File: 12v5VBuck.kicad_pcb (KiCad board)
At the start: 4 copper layers, 20.5 x 26 mm, 17 parts, among them IC1 TPS54302DDCT, J1 Conn_01x02, J2 Conn_01x02

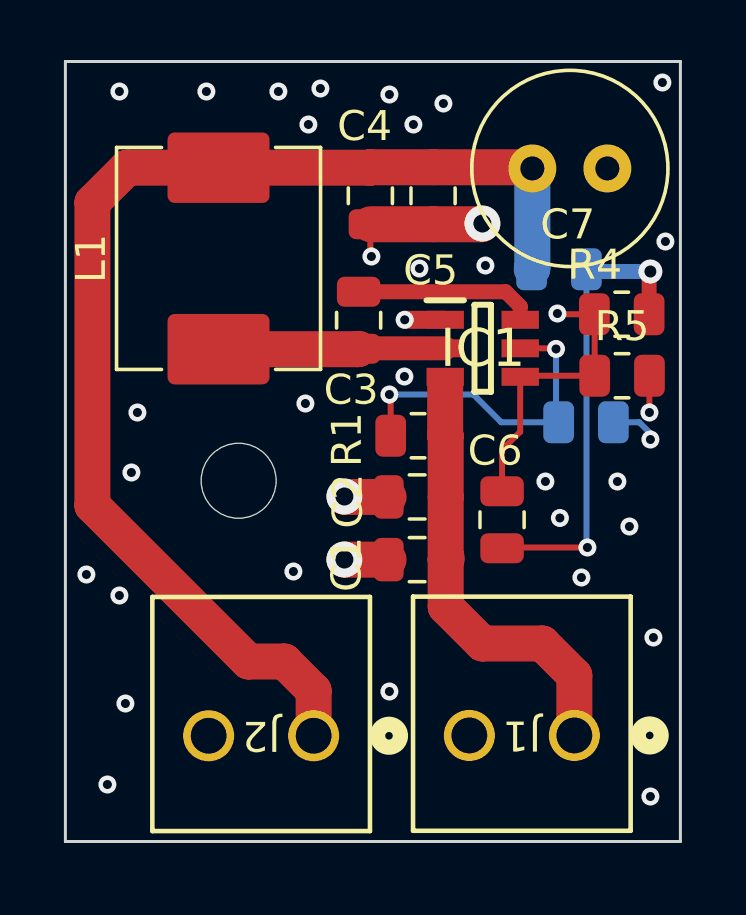
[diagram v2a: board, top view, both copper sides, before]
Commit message: Minor changes to traces
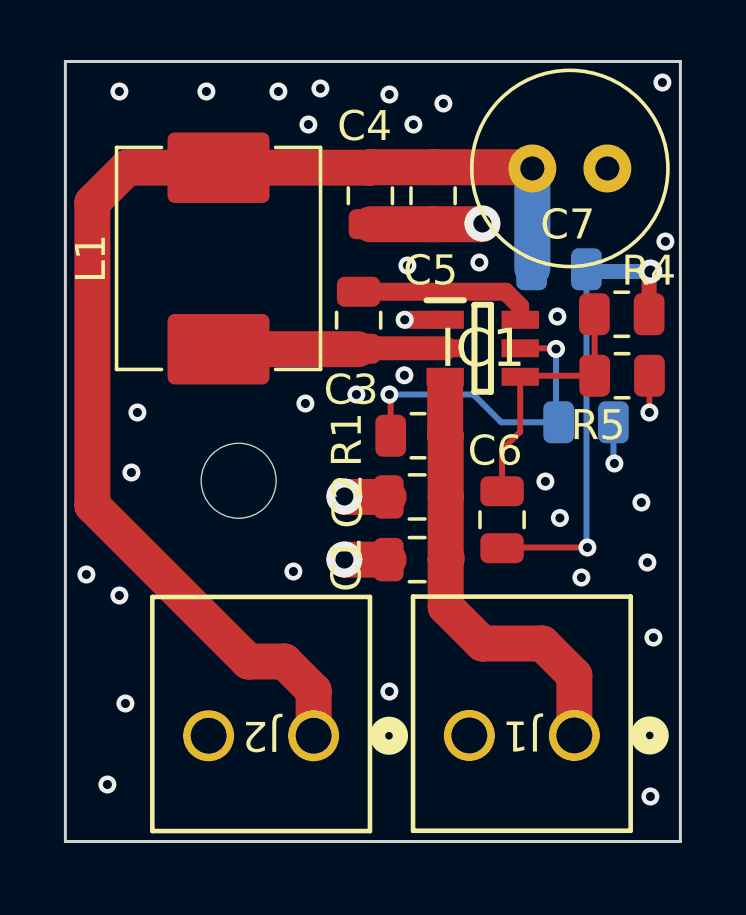
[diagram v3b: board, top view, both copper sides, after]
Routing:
- net Net-(IC1-FB): track 9.86 -> 8.60 mm, vias 1 -> 0
- net GND: track 11.9 -> 10.7 mm, vias 36 -> 37
- net Net-(IC1-BOOT): track 5.54 -> 6.04 mm
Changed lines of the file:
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@@
     (property "ki_keywords" "r resistor")
     (attr smd)
-    (fp_text reference "R5" (at 0 -1.65) (layer "F.SilkS")
+    (fp_text reference "R5" (at -0.8 1.65) (layer "F.SilkS")
         (effects (font (size 1 1) (thickness 0.15)))
     )
@@
       (rotate (xyz 0 0 0))
     )
+    (model "C:/Users/Sylvester Pudelko/Documents/KiCad/7.0/3dmodels/DDC0006A.stp"
+      (offset (xyz 0 0 0))
+      (scale (xyz 1 1 1))
+      (rotate (xyz 0 0 0))
+    )
   )
   (footprint "Capacitor_SMD:C_0805_2012Metric" (layer "F.Cu")
@@
     (property "ki_keywords" "r resistor")
     (attr smd)
-    (fp_text reference "R4" (at 0.9 1.65) (layer "F.SilkS")
+    (fp_text reference "R4" (at -0.9 1.45) (layer "F.SilkS")
         (effects (font (size 1 1) (thickness 0.15)))
     )
@@
   (segment (start 63.815 29.115) (end 63.8 29.1) (width 1.2) (layer "F.Cu") (net 2))
   (segment (start 66.755 20.025) (end 68.375 20.025) (width 1.2) (layer "F.Cu") (net 2))
-  (segment (start 64.665 20.025) (end 64.665 21.065) (width 0.2) (layer "F.Cu") (net 2))
   (segment (start 68.375 20.025) (end 68.4 20) (width 1.2) (layer "F.Cu") (net 2))
   (segment (start 73.9675 26.3) (end 73.9675 25.075) (width 0.2) (layer "F.Cu") (net 2))
@@
   (segment (start 63.805 31.205) (end 63.8 31.2) (width 1.2) (layer "F.Cu") (net 2))
   (segment (start 65.275 31.205) (end 63.805 31.205) (width 1.2) (layer "F.Cu") (net 2))
-  (via (at 65.8 25.1) (size 0.6) (drill 0.3) (layers "F.Cu" "B.Cu") (net 2))
-  (via (at 66.3 21.5) (size 0.6) (drill 0.3) (layers "F.Cu" "B.Cu") (net 2))
+  (via (at 65.8 25.0595) (size 0.6) (drill 0.3) (layers "F.Cu" "B.Cu") (net 2))
   (via (at 56.9 26.3) (size 0.6) (drill 0.3) (layers "F.Cu" "B.Cu") (net 2))
   (via (at 56.3 15.6) (size 0.6) (drill 0.3) (layers "F.Cu" "B.Cu") (net 2))
+  (via (at 70.9 23.1) (size 0.6) (drill 0.3) (layers "F.Cu" "B.Cu") (net 2))
   (via (at 65.81 23.21) (size 0.6) (drill 0.3) (layers "F.Cu" "B.Cu") (net 2))
   (via (at 56.7 28.3) (size 0.6) (drill 0.3) (layers "F.Cu" "B.Cu") (net 2))
@@
   (via (at 62.1 31.6) (size 0.6) (drill 0.3) (layers "F.Cu" "B.Cu") (net 2))
   (via (at 74 39.1) (size 0.6) (drill 0.3) (layers "F.Cu" "B.Cu") (net 2))
-  (via (at 68.5 21.4) (size 0.6) (drill 0.3) (layers "F.Cu" "B.Cu") (net 2))
   (via (at 67.1 16) (size 0.6) (drill 0.3) (layers "F.Cu" "B.Cu") (net 2))
-  (via (at 72.9 28.6) (size 0.6) (drill 0.3) (layers "F.Cu" "B.Cu") (net 2))
+  (via (at 73.7 29.3) (size 0.6) (drill 0.3) (layers "F.Cu" "B.Cu") (net 2))
   (via (at 74.4 15.3) (size 0.6) (drill 0.3) (layers "F.Cu" "B.Cu") (net 2))
+  (via (at 65.9 21.4) (size 0.6) (drill 0.3) (layers "F.Cu" "B.Cu") (net 2))
   (via (at 70.5 28.6) (size 0.6) (drill 0.3) (layers "F.Cu" "B.Cu") (net 2))
   (via (at 66.1 16.7) (size 0.6) (drill 0.3) (layers "F.Cu" "B.Cu") (net 2))
-  (via (at 73.3 30.1) (size 0.6) (drill 0.3) (layers "F.Cu" "B.Cu") (net 2))
+  (via (at 73.9 31.3) (size 0.6) (drill 0.3) (layers "F.Cu" "B.Cu") (net 2))
   (via (at 63.8 29.1) (size 1.2) (drill 0.6) (layers "F.Cu" "B.Cu") (net 2))
+  (via (at 64.2 25.7) (size 0.6) (drill 0.3) (layers "F.Cu" "B.Cu") (net 2))
   (via (at 55.2 31.7) (size 0.6) (drill 0.3) (layers "F.Cu" "B.Cu") (net 2))
   (via (at 63.8 31.2) (size 1.2) (drill 0.6) (layers "F.Cu" "B.Cu") (net 2))
   (via (at 61.6 15.6) (size 0.6) (drill 0.3) (layers "F.Cu" "B.Cu") (net 2))
-  (via (at 74 27.2) (size 0.6) (drill 0.3) (layers "F.Cu" "B.Cu") (net 2))
+  (via (at 72.8 28) (size 0.6) (drill 0.3) (layers "F.Cu" "B.Cu") (net 2))
   (via (at 62.5 26) (size 0.6) (drill 0.3) (layers "F.Cu" "B.Cu") (net 2))
-  (via (at 64.7 21.1) (size 0.6) (drill 0.3) (layers "F.Cu" "B.Cu") (net 2))
   (via (at 74.1 33.8) (size 0.6) (drill 0.3) (layers "F.Cu" "B.Cu") (net 2))
   (via (at 56.5 36) (size 0.6) (drill 0.3) (layers "F.Cu" "B.Cu") (net 2))
@@
   (via (at 65.3 35.6) (size 0.6) (drill 0.3) (layers "F.Cu" "B.Cu") (net 2))
   (via (at 59.2 15.6) (size 0.6) (drill 0.3) (layers "F.Cu" "B.Cu") (net 2))
+  (via (at 68.3 21.3) (size 0.6) (drill 0.3) (layers "F.Cu" "B.Cu") (net 2))
   (via (at 73.9675 26.3) (size 0.6) (drill 0.3) (layers "F.Cu" "B.Cu") (net 2))
   (via (at 74.5 20.6) (size 0.6) (drill 0.3) (layers "F.Cu" "B.Cu") (net 2))
   (via (at 65.3 15.7) (size 0.6) (drill 0.3) (layers "F.Cu" "B.Cu") (net 2))
-  (segment (start 73.625 26.625) (end 74 27) (width 0.2) (layer "B.Cu") (net 2))
-  (segment (start 74 27) (end 74 27.2) (width 0.2) (layer "B.Cu") (net 2))
-  (segment (start 72.7675 26.625) (end 73.625 26.625) (width 0.2) (layer "B.Cu") (net 2))
-  (segment (start 69.66 22.76) (end 69.175 22.275) (width 0.5) (layer "F.Cu") (net 3))
-  (segment (start 69.175 22.275) (end 64.775 22.275) (width 0.5) (layer "F.Cu") (net 3))
-  (segment (start 69.66 23.21) (end 69.66 22.76) (width 0.5) (layer "F.Cu") (net 3))
-  (segment (start 67.16 24.16) (end 64.79 24.16) (width 0.8) (layer "F.Cu") (net 4))
-  (segment (start 64.79 24.16) (end 64.775 24.175) (width 0.8) (layer "F.Cu") (net 4))
-  (segment (start 64.26 24.19) (end 64.275 24.175) (width 1.2) (layer "F.Cu") (net 4))
+  (segment (start 72.8 28) (end 72.7675 27.9675) (width 0.2) (layer "B.Cu") (net 2))
+  (segment (start 72.7675 27.9675) (end 72.7675 26.625) (width 0.2) (layer "B.Cu") (net 2))
+  (segment (start 64.275 22.275) (end 69.175 22.275) (width 0.6) (layer "F.Cu") (net 3))
+  (segment (start 69.175 22.275) (end 69.66 22.76) (width 0.6) (layer "F.Cu") (net 3))
+  (segment (start 69.66 22.76) (end 69.66 23.21) (width 0.6) (layer "F.Cu") (net 3))
   (segment (start 59.605 24.19) (end 64.26 24.19) (width 1.2) (layer "F.Cu") (net 4))
-  (segment (start 59.92 24.175) (end 59.905 24.19) (width 1.2) (layer "F.Cu") (net 4))
+  (segment (start 67.16 24.16) (end 64.29 24.16) (width 0.8) (layer "F.Cu") (net 4))
   (segment (start 73.9575 23.025) (end 73.9575 21.6425) (width 0.5) (layer "F.Cu") (net 5))
   (segment (start 69.08 30.8) (end 69.055 30.825) (width 0.2) (layer "F.Cu") (net 5))
@@
   (segment (start 72.1425 21.6) (end 71.8675 21.325) (width 0.5) (layer "B.Cu") (net 5))
   (segment (start 69.695 25.075) (end 69.66 25.11) (width 0.2) (layer "F.Cu") (net 6))
-  (segment (start 70.925 23.025) (end 70.9 23) (width 0.2) (layer "F.Cu") (net 6))
   (segment (start 69.055 28.925) (end 69.055 27.545) (width 0.2) (layer "F.Cu") (net 6))
   (segment (start 69.66 26.94) (end 69.66 25.11) (width 0.2) (layer "F.Cu") (net 6))
   (segment (start 69.055 27.545) (end 69.66 26.94) (width 0.2) (layer "F.Cu") (net 6))
-  (segment (start 72.1325 23.025) (end 70.925 23.025) (width 0.2) (layer "F.Cu") (net 6))
   (segment (start 72.1425 25.075) (end 72.1425 23.035) (width 0.2) (layer "F.Cu") (net 6))
   (segment (start 72.1425 25.075) (end 69.695 25.075) (width 0.2) (layer "F.Cu") (net 6))
-  (segment (start 72.1425 23.035) (end 72.1325 23.025) (width 0.2) (layer "F.Cu") (net 6))
-  (via (at 70.9 23) (size 0.6) (drill 0.3) (layers "F.Cu" "B.Cu") (net 6))
   (segment (start 70.8546 24.181601) (end 70.832999 24.16) (width 0.2) (layer "F.Cu") (net 7))
   (segment (start 65.3425 27.075) (end 65.3425 25.7425) (width 0.2) (layer "F.Cu") (net 7))
@@
   (via (at 70.8546 24.181601) (size 0.6) (drill 0.3) (layers "F.Cu" "B.Cu") (net 7))
   (via (at 65.3 25.7) (size 0.6) (drill 0.3) (layers "F.Cu" "B.Cu") (net 7))
-  (segment (start 70.8546 24.181601) (end 70.8546 26.4371) (width 0.2) (layer "B.Cu") (net 7))
   (segment (start 65.3 25.7) (end 68.1 25.7) (width 0.2) (layer "B.Cu") (net 7))
   (segment (start 68.1 25.7) (end 69.025 26.625) (width 0.2) (layer "B.Cu") (net 7))
-  (segment (start 70.8546 26.4371) (end 71.0425 26.625) (width 0.2) (layer "B.Cu") (net 7))
   (segment (start 69.025 26.625) (end 70.9425 26.625) (width 0.2) (layer "B.Cu") (net 7))
+  (segment (start 70.8546 24.181601) (end 70.8546 26.5371) (width 0.2) (layer "B.Cu") (net 7))
   (segment (start 61.8 34.6) (end 60.6 34.6) (width 1.2) (layer "F.Cu") (net 8))
   (segment (start 64.65 18.14) (end 64.665 18.125) (width 1.2) (layer "F.Cu") (net 8))
@@
   (segment (start 70.025 18.125) (end 70.065 18.165) (width 1.2) (layer "F.Cu") (net 8))
   (segment (start 64.665 18.125) (end 66.755 18.125) (width 1.2) (layer "F.Cu") (net 8))
-  (segment (start 70.065 21.5025) (end 70.0425 21.525) (width 1.2) (layer "B.Cu") (net 8))
   (segment (start 70.065 18.165) (end 70.065 21.5025) (width 1.2) (layer "B.Cu") (net 8))
   (zone (net 2) (net_name "GND") (layers "In1.Cu" "In2.Cu") (hatch edge 0.5)
     (connect_pads (clearance 0.5))
     (min_thickness 0.25) (filled_areas_thickness no)
-    (fill (thermal_gap 0.5) (thermal_bridge_width 0.5) (island_removal_mode 1) (island_area_min 10))
+    (fill yes (thermal_gap 0.5) (thermal_bridge_width 0.5) (island_removal_mode 1) (island_area_min 10))
     (polygon
       (pts

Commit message: Changed capacitor type for 47uF capacitor
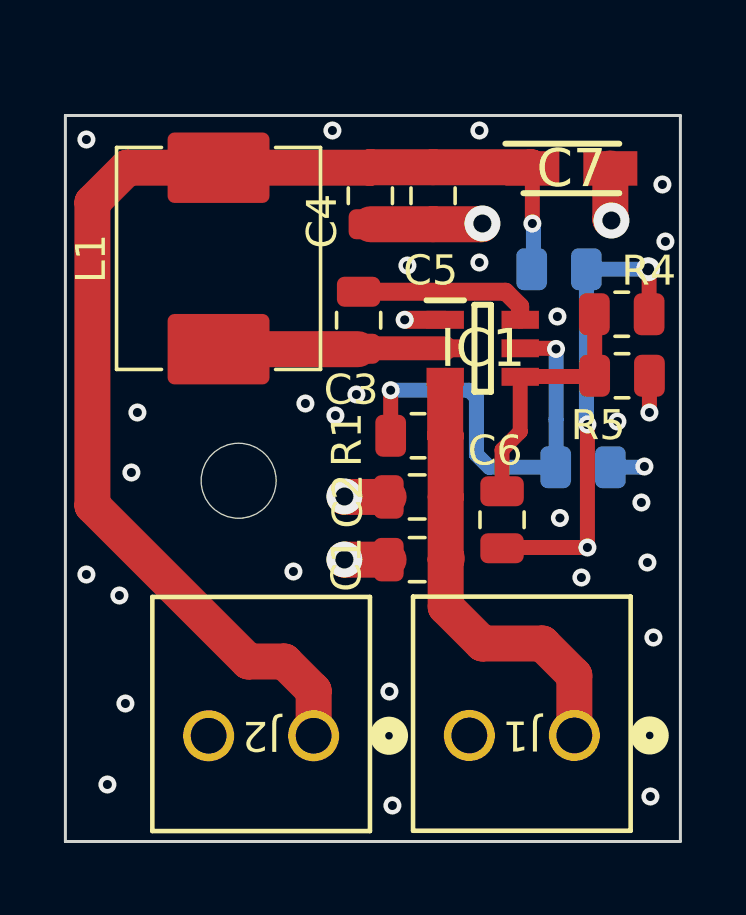
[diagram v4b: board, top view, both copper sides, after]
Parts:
- C7: footprint Capacitor_THT:C_Radial_D6.3mm_H11.0mm_P2.50mm -> footprints:CAPPM3216X180N
- moved R2 1.50 mm to (71.8, 28.1)
- moved C7 1.30 mm to (71.4, 18.2)
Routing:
- net Net-(IC1-EN): track 11.1 -> 14.4 mm
- net GND: track 10.7 -> 12.2 mm, vias 37 -> 34
- net Net-(C6-Pad1): vias 2 -> 3
- net +5V: vias 0 -> 1
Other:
- board size 20.5 x 26 mm -> 20.5 x 24.2 mm

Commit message: Changed resistor to front
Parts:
- R3: moved to F.Cu
- moved R3 1.10 mm to (71.0, 20.4)
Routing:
- net Net-(C6-Pad1): track 15.8 -> 17.9 mm, vias 3 -> 2
- net +5V: track 39.7 -> 38.6 mm, vias 1 -> 0
- net GND: track 12.2 -> 12.0 mm, vias 34 -> 33
